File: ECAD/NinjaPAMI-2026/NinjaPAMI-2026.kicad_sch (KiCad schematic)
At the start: 62 parts, among them J1 Con_Batt, J11 Conn_01x04, J12 OLED, J13 RightMotor, J14 LeftMotor, J15 BAU, J2 Servo, J3 Servo, J4 Sensor_RIGHT, J5 Sensor_Center, J6 Sensor_LEFT, J7 Conn_01x04, J8 Conn_01x04, SW3 SW_SPDT, U1 R-78E5.0-1.0, U2 XIAO-HALF-HOLE-23P, U3 TMC2209_SILENTSTEPSTICK, U4 TMC2209_SILENTSTEPSTICK, U5 DRV5023, U6 R-78B5.0-2.0, U7 R-78B5.0-2.0

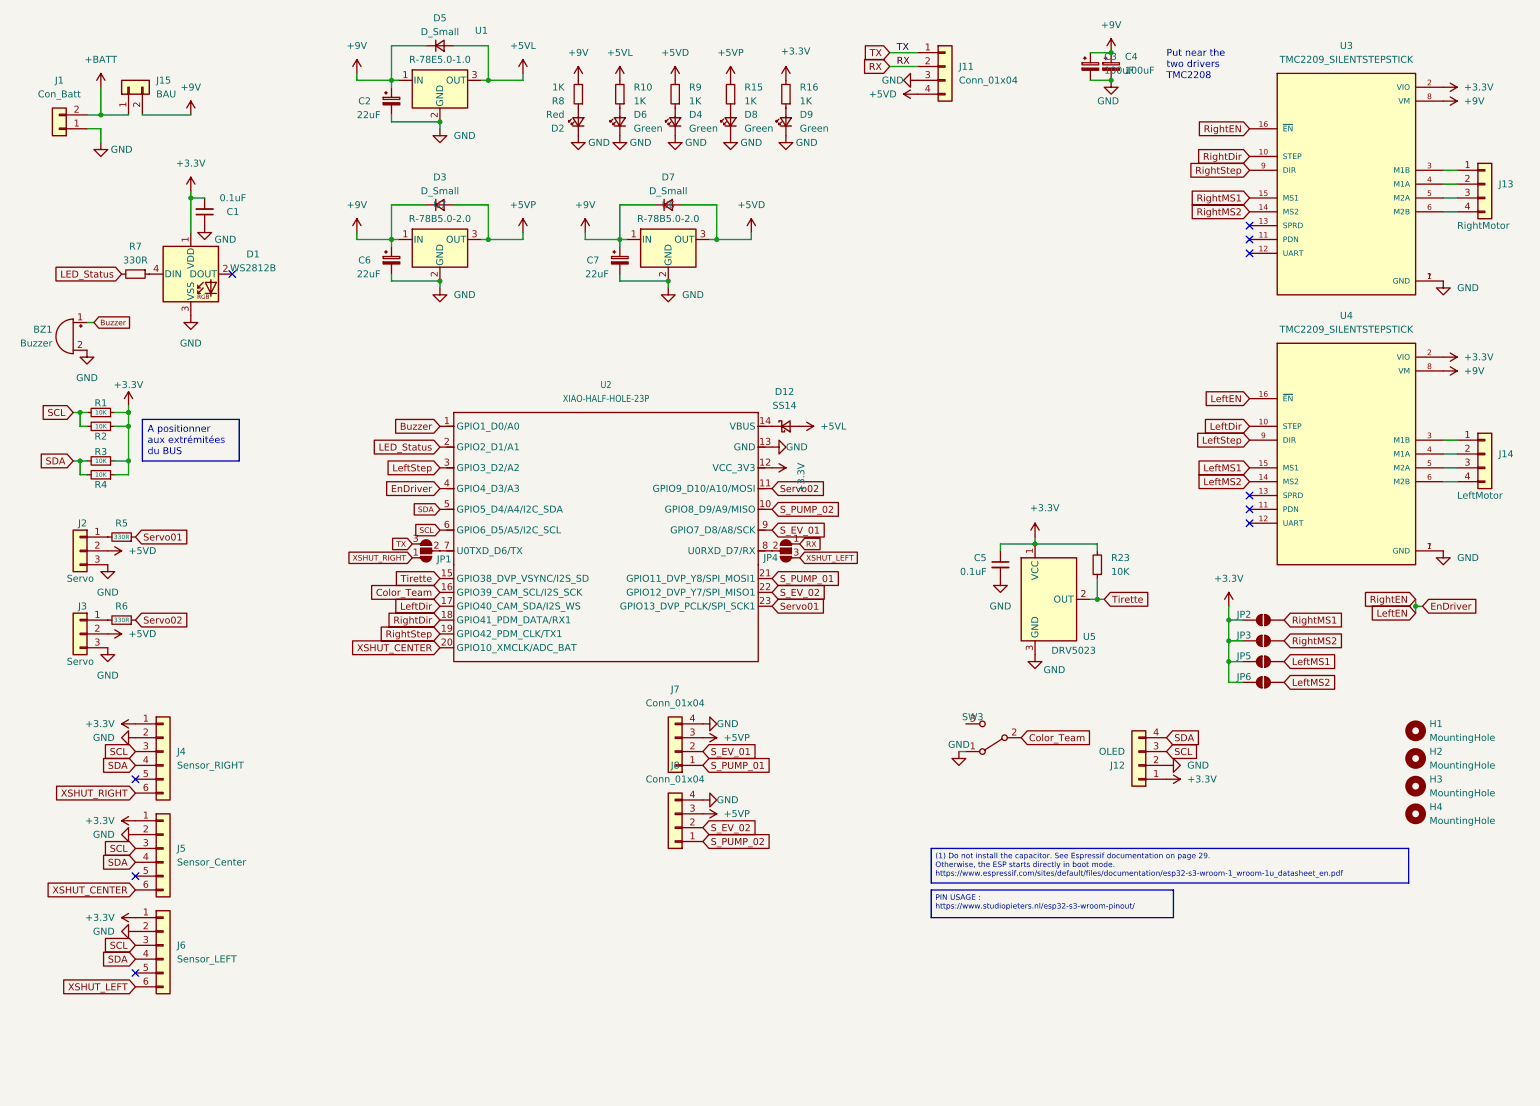
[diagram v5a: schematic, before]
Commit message: fix driver inverted issue
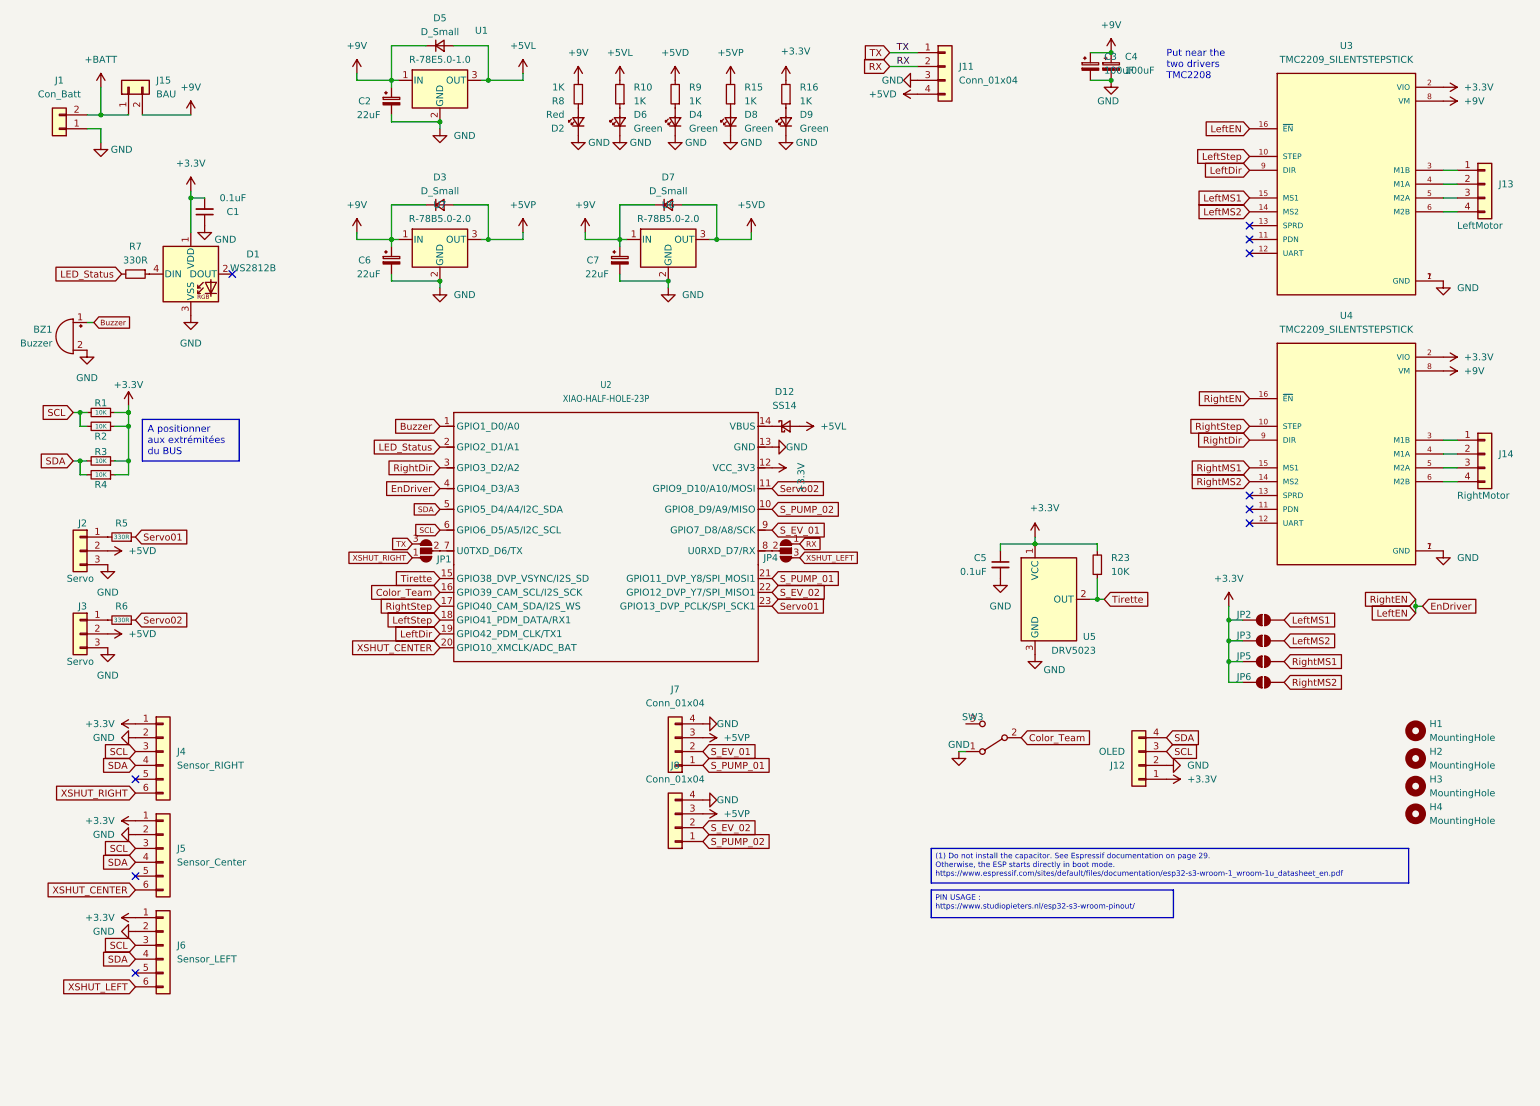
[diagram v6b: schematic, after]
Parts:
- J13: value RightMotor -> LeftMotor
- J14: value LeftMotor -> RightMotor
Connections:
- net LeftDir: now also U2.19 (GPIO42_PDM_CLK/TX1), U3.9 (DIR); no longer U2.17 (GPIO40_CAM_SDA/I2S_WS), U4.10 (STEP)
- net LeftMS1: now also JP2.2 (B), U3.15 (MS1); no longer JP5.2 (B), U4.15 (MS1)
- net LeftMS2: now also JP3.2 (B), U3.14 (MS2); no longer JP6.2 (B), U4.14 (MS2)
- net LeftStep: now also U2.18 (GPIO41_PDM_DATA/RX1), U3.10 (STEP); no longer U2.3 (GPIO3_D2/A2), U4.9 (DIR)
- net RightDir: now also U2.3 (GPIO3_D2/A2), U4.9 (DIR); no longer U2.18 (GPIO41_PDM_DATA/RX1), U3.10 (STEP)
- net RightMS1: now also JP5.2 (B), U4.15 (MS1); no longer JP2.2 (B), U3.15 (MS1)
- net RightMS2: now also JP6.2 (B), U4.14 (MS2); no longer JP3.2 (B), U3.14 (MS2)
- net RightStep: now also U2.17 (GPIO40_CAM_SDA/I2S_WS), U4.10 (STEP); no longer U2.19 (GPIO42_PDM_CLK/TX1), U3.9 (DIR)
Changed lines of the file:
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@@
 	(global_label "RightMS1"
 		(shape input)
-		(at 236.22 48.26 180)
+		(at 236.22 97.79 180)
 		(fields_autoplaced yes)
 		(effects
@@
 		)
 		(property "Intersheetrefs" "${INTERSHEET_REFS}"
-			(at 224.4659 48.26 0)
+			(at 224.4659 97.79 0)
 			(effects
 				(font
@@
 	(global_label "LeftEN"
 		(shape input)
-		(at 236.22 85.09 180)
+		(at 236.22 35.56 180)
 		(fields_autoplaced yes)
 		(effects
@@
 		)
 		(property "Intersheetrefs" "${INTERSHEET_REFS}"
-			(at 227.1872 85.09 0)
+			(at 227.1872 35.56 0)
 			(effects
 				(font
@@
 	(global_label "LeftDir"
 		(shape input)
-		(at 236.22 90.17 180)
+		(at 236.22 43.18 180)
 		(fields_autoplaced yes)
 		(effects
@@
 		)
 		(property "Intersheetrefs" "${INTERSHEET_REFS}"
-			(at 227.0057 90.17 0)
+			(at 227.0057 43.18 0)
 			(effects
 				(font
@@
 	(global_label "LeftMS2"
 		(shape input)
-		(at 236.22 100.33 180)
+		(at 236.22 50.8 180)
 		(fields_autoplaced yes)
 		(effects
@@
 		)
 		(property "Intersheetrefs" "${INTERSHEET_REFS}"
-			(at 225.7963 100.33 0)
+			(at 225.7963 50.8 0)
 			(effects
 				(font
@@
 	(global_label "RightEN"
 		(shape input)
-		(at 236.22 35.56 180)
+		(at 236.22 85.09 180)
 		(fields_autoplaced yes)
 		(effects
@@
 		)
 		(property "Intersheetrefs" "${INTERSHEET_REFS}"
-			(at 225.8568 35.56 0)
+			(at 225.8568 85.09 0)
 			(effects
 				(font
@@
 	(global_label "RightMS1"
 		(shape input)
-		(at 242.57 125.73 0)
+		(at 242.57 133.35 0)
 		(fields_autoplaced yes)
 		(effects
@@
 		)
 		(property "Intersheetrefs" "${INTERSHEET_REFS}"
-			(at 254.3241 125.73 0)
+			(at 254.3241 133.35 0)
 			(effects
 				(font
@@
 	(global_label "RightMS2"
 		(shape input)
-		(at 242.57 129.54 0)
+		(at 242.57 137.16 0)
 		(fields_autoplaced yes)
 		(effects
@@
 		)
 		(property "Intersheetrefs" "${INTERSHEET_REFS}"
-			(at 254.3241 129.54 0)
+			(at 254.3241 137.16 0)
 			(effects
 				(font
@@
 	(global_label "LeftStep"
 		(shape input)
-		(at 236.22 92.71 180)
+		(at 236.22 40.64 180)
 		(fields_autoplaced yes)
 		(effects
@@
 		)
 		(property "Intersheetrefs" "${INTERSHEET_REFS}"
-			(at 225.4939 92.71 0)
+			(at 225.4939 40.64 0)
 			(effects
 				(font
@@
 	(global_label "RightMS2"
 		(shape input)
-		(at 236.22 50.8 180)
+		(at 236.22 100.33 180)
 		(fields_autoplaced yes)
 		(effects
@@
 		)
 		(property "Intersheetrefs" "${INTERSHEET_REFS}"
-			(at 224.4659 50.8 0)
+			(at 224.4659 100.33 0)
 			(effects
 				(font
@@
 	(global_label "LeftMS1"
 		(shape input)
-		(at 242.57 133.35 0)
+		(at 242.57 125.73 0)
 		(fields_autoplaced yes)
 		(effects
@@
 		)
 		(property "Intersheetrefs" "${INTERSHEET_REFS}"
-			(at 252.9937 133.35 0)
+			(at 252.9937 125.73 0)
 			(effects
 				(font
@@
 	(global_label "LeftStep"
 		(shape input)
-		(at 87.63 97.79 180)
+		(at 87.63 125.73 180)
 		(fields_autoplaced yes)
 		(effects
@@
 		)
 		(property "Intersheetrefs" "${INTERSHEET_REFS}"
-			(at 76.9039 97.79 0)
+			(at 76.9039 125.73 0)
 			(effects
 				(font
@@
 	(global_label "LeftMS2"
 		(shape input)
-		(at 242.57 137.16 0)
+		(at 242.57 129.54 0)
 		(fields_autoplaced yes)
 		(effects
@@
 		)
 		(property "Intersheetrefs" "${INTERSHEET_REFS}"
-			(at 252.9937 137.16 0)
+			(at 252.9937 129.54 0)
 			(effects
 				(font
@@
 	(global_label "RightStep"
 		(shape input)
-		(at 87.63 128.27 180)
+		(at 87.63 123.19 180)
 		(fields_autoplaced yes)
 		(effects
@@
 		)
 		(property "Intersheetrefs" "${INTERSHEET_REFS}"
-			(at 75.5735 128.27 0)
+			(at 75.5735 123.19 0)
 			(effects
 				(font
@@
 	(global_label "RightDir"
 		(shape input)
-		(at 87.63 125.73 180)
+		(at 87.63 97.79 180)
 		(fields_autoplaced yes)
 		(effects
@@
 		)
 		(property "Intersheetrefs" "${INTERSHEET_REFS}"
-			(at 77.0853 125.73 0)
+			(at 77.0853 97.79 0)
 			(effects
 				(font
@@
 	(global_label "RightDir"
 		(shape input)
-		(at 236.22 40.64 180)
+		(at 236.22 92.71 180)
 		(fields_autoplaced yes)
 		(effects
@@
 		)
 		(property "Intersheetrefs" "${INTERSHEET_REFS}"
-			(at 225.6753 40.64 0)
+			(at 225.6753 92.71 0)
 			(effects
 				(font
@@
 	(global_label "LeftDir"
 		(shape input)
-		(at 87.63 123.19 180)
+		(at 87.63 128.27 180)
 		(fields_autoplaced yes)
 		(effects
@@
 		)
 		(property "Intersheetrefs" "${INTERSHEET_REFS}"
-			(at 78.4157 123.19 0)
+			(at 78.4157 128.27 0)
 			(effects
 				(font
@@
 	(global_label "RightStep"
 		(shape input)
-		(at 236.22 43.18 180)
+		(at 236.22 90.17 180)
 		(fields_autoplaced yes)
 		(effects
@@
 		)
 		(property "Intersheetrefs" "${INTERSHEET_REFS}"
-			(at 224.1635 43.18 0)
+			(at 224.1635 90.17 0)
 			(effects
 				(font
@@
 	(global_label "LeftMS1"
 		(shape input)
-		(at 236.22 97.79 180)
+		(at 236.22 48.26 180)
 		(fields_autoplaced yes)
 		(effects
@@
 		)
 		(property "Intersheetrefs" "${INTERSHEET_REFS}"
-			(at 225.7963 97.79 0)
+			(at 225.7963 48.26 0)
 			(effects
 				(font
@@
 			)
 		)
-		(property "Value" "LeftMotor"
+		(property "Value" "RightMotor"
 			(at 274.32 102.87 0)
 			(effects
@@
 			)
 		)
-		(property "Value" "RightMotor"
+		(property "Value" "LeftMotor"
 			(at 274.32 53.34 0)
 			(effects
